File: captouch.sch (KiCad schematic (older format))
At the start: 39 parts, among them J401 MOLEX_502250-8037, J402 MOLEX_502250-8037, U401 FT5816LPC, X401 12MHz 18pF

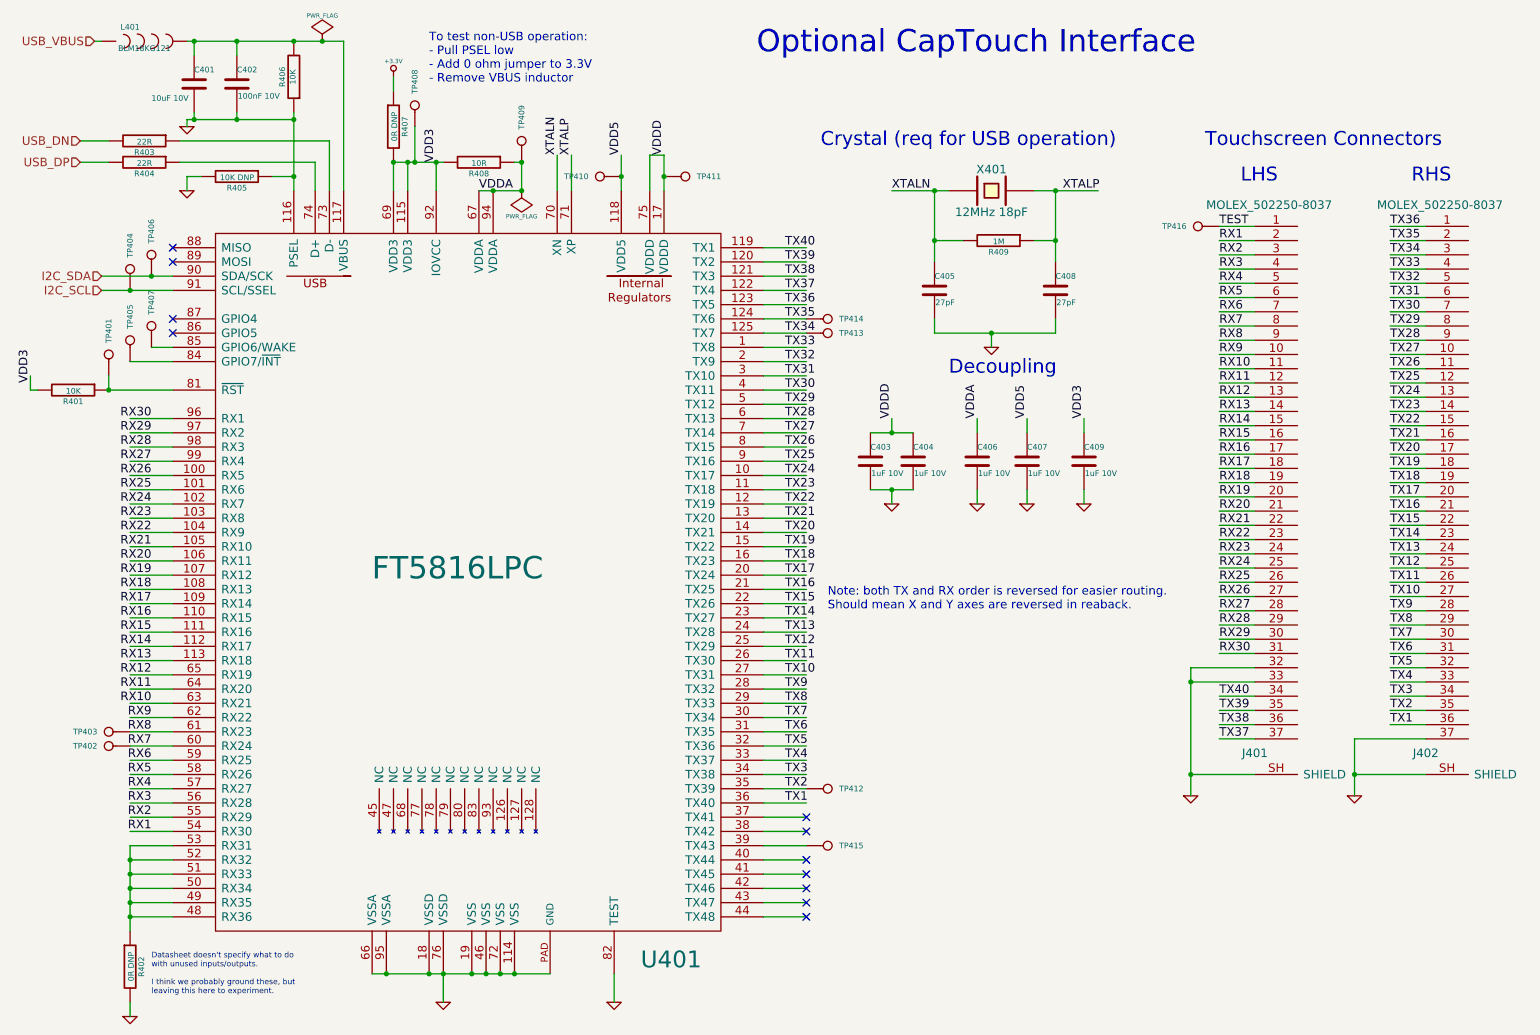
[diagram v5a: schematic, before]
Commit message: Routed, passes DRC
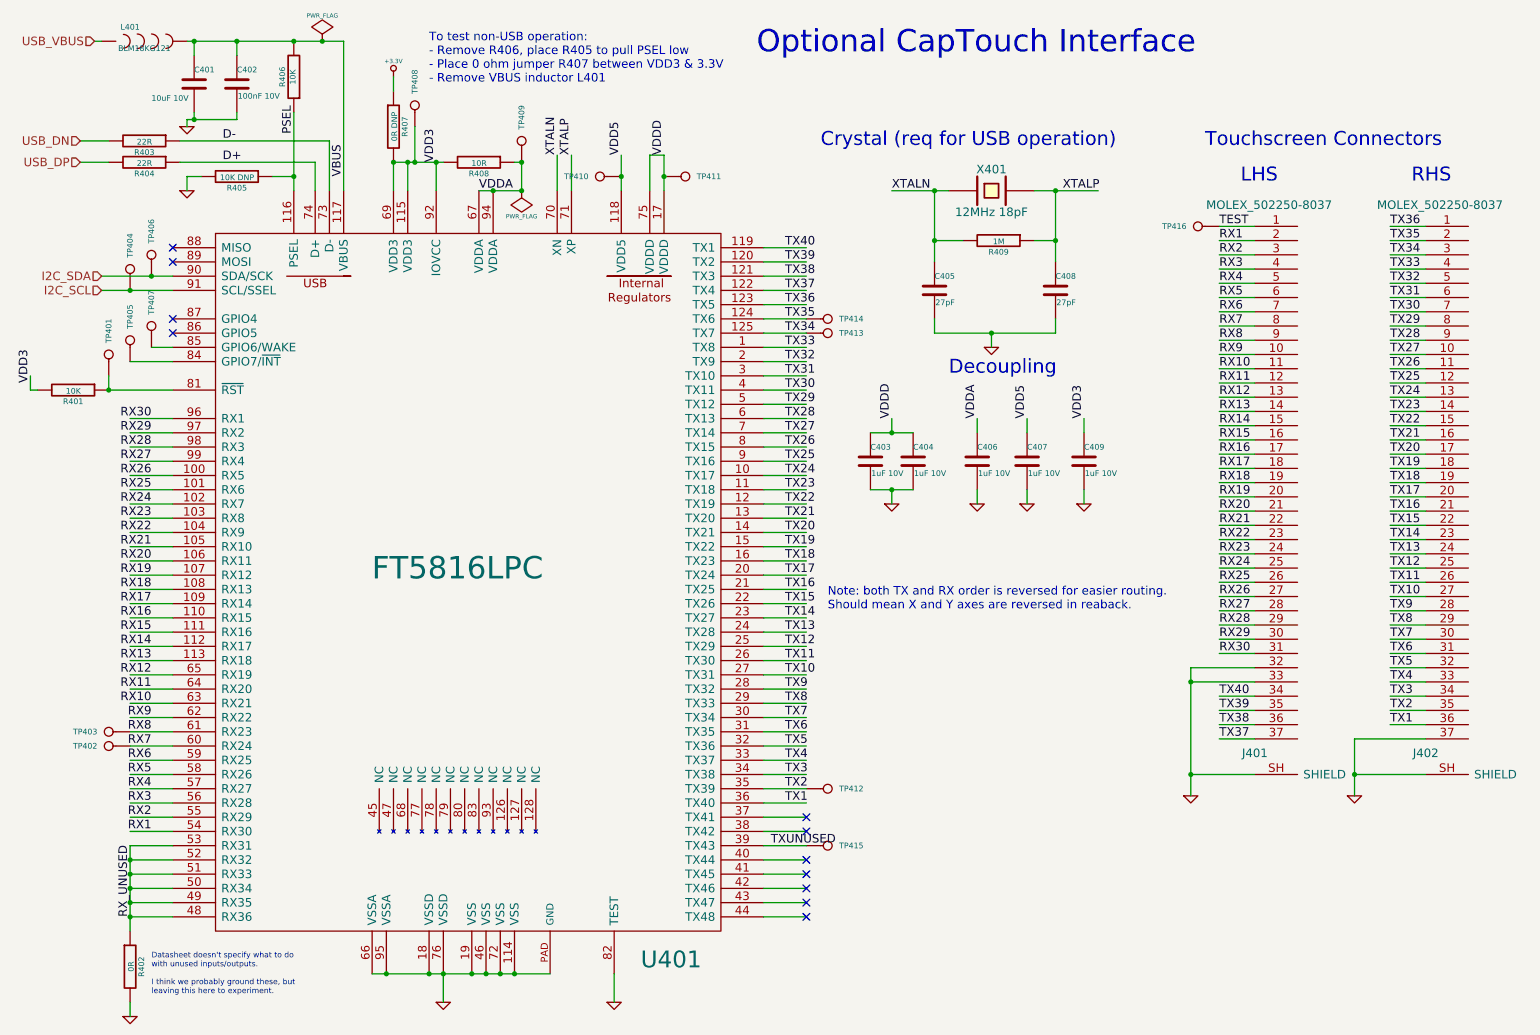
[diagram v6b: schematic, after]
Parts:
- C402: footprint SMD_Packages:SMD-0402_c -> FT:C0402
- C403, C404, C406, C407, C409: footprint FT:1206 -> FT:0603
- R402: value 0R DNP -> 0R
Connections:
- net labels added: D+, D-, PSEL, RX_UNUSED, TXUNUSED, VBUS
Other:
- note added: "To test non-USB operation:\n- Remove R406, place R405 to pull PSEL low\n- Place 0 ohm jumper R407 between VDD3 & 3.3V\n- Remove VBUS inductor L401"
- note removed: "To test non-USB operation:\n- Pull PSEL low\n- Add 0 ohm jumper to 3.3V\n- Remove VBUS inductor"
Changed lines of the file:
@@
 F 0 "C403" H 6600 3800 40  0000 L CNN
 F 1 "1uF 10V" H 6606 3615 40  0000 L CNN
-F 2 "FT:1206" H 6638 3550 30  0001 C CNN
+F 2 "FT:0603" H 6638 3550 30  0001 C CNN
 F 3 "" H 6600 3700 60  0000 C CNN
 	1    6600 3700
@@
 F 0 "C407" H 7700 3800 40  0000 L CNN
 F 1 "1uF 10V" H 7706 3615 40  0000 L CNN
-F 2 "FT:1206" H 7738 3550 30  0001 C CNN
+F 2 "FT:0603" H 7738 3550 30  0001 C CNN
 F 3 "" H 7700 3700 60  0000 C CNN
 	1    7700 3700
@@
 F 0 "C406" H 7350 3800 40  0000 L CNN
 F 1 "1uF 10V" H 7356 3615 40  0000 L CNN
-F 2 "FT:1206" H 7388 3550 30  0001 C CNN
+F 2 "FT:0603" H 7388 3550 30  0001 C CNN
 F 3 "" H 7350 3700 60  0000 C CNN
 	1    7350 3700
@@
 F 0 "C409" H 8100 3800 40  0000 L CNN
 F 1 "1uF 10V" H 8106 3615 40  0000 L CNN
-F 2 "FT:1206" H 8138 3550 30  0001 C CNN
+F 2 "FT:0603" H 8138 3550 30  0001 C CNN
 F 3 "" H 8100 3700 60  0000 C CNN
 	1    8100 3700
@@
 F 0 "C404" H 6900 3800 40  0000 L CNN
 F 1 "1uF 10V" H 6906 3615 40  0000 L CNN
-F 2 "FT:1206" H 6938 3550 30  0001 C CNN
+F 2 "FT:0603" H 6938 3550 30  0001 C CNN
 F 3 "" H 6900 3700 60  0000 C CNN
 	1    6900 3700
@@
 F 0 "C402" H 2150 1150 40  0000 L CNN
 F 1 "100nF 10V" H 2156 965 40  0000 L CNN
-F 2 "SMD_Packages:SMD-0402_c" H 2188 900 30  0001 C CNN
+F 2 "FT:C0402" H 2188 900 30  0001 C CNN
 F 3 "" H 2150 1050 60  0000 C CNN
 	1    2150 1050
@@
 	2150 750  2150 850
 Wire Wire Line
-	1800 1300 2550 1300
-Wire Wire Line
 	2150 1300 2150 1250
 Wire Wire Line
 	1850 1300 1850 1250
-Connection ~ 2150 1300
 Wire Wire Line
 	1800 1300 1800 1350
@@
 Wire Wire Line
 	1750 1450 2800 1450
-Connection ~ 2550 1300
 Wire Wire Line
 	700  3200 750  3200
@@
 RHS
 Text Notes 3500 1050 0    60   ~ 0
-To test non-USB operation:\n- Pull PSEL low\n- Add 0 ohm jumper to 3.3V\n- Remove VBUS inductor
+To test non-USB operation:\n- Remove R406, place R405 to pull PSEL low\n- Place 0 ohm jumper R407 between VDD3 & 3.3V\n- Remove VBUS inductor L401
 $Comp
 L FT5816LPC U401
@@
 P 1400 7250
 F 0 "R402" V 1480 7250 40  0000 C CNN
-F 1 "0R DNP" V 1407 7251 40  0000 C CNN
+F 1 "0R" V 1407 7251 40  0000 C CNN
 F 2 "FT:0603" V 1330 7250 30  0001 C CNN
 F 3 "" H 1400 7250 30  0000 C CNN
@@
 Text Notes 6300 4750 0    60   ~ 0
 Note: both TX and RX order is reversed for easier routing.\nShould mean X and Y axes are reversed in reaback.
+Wire Wire Line
+	1800 1300 2150 1300
+Text Label 2550 1400 1    60   ~ 0
+PSEL
+Text Label 2900 1700 1    60   ~ 0
+VBUS
+Text Label 2050 1450 0    60   ~ 0
+D-
+Text Label 2050 1600 0    60   ~ 0
+D+
+Text Label 1400 6900 1    60   ~ 0
+RX_UNUSED
+Text Label 5900 6400 0    60   ~ 0
+TXUNUSED
 $EndSCHEMATC

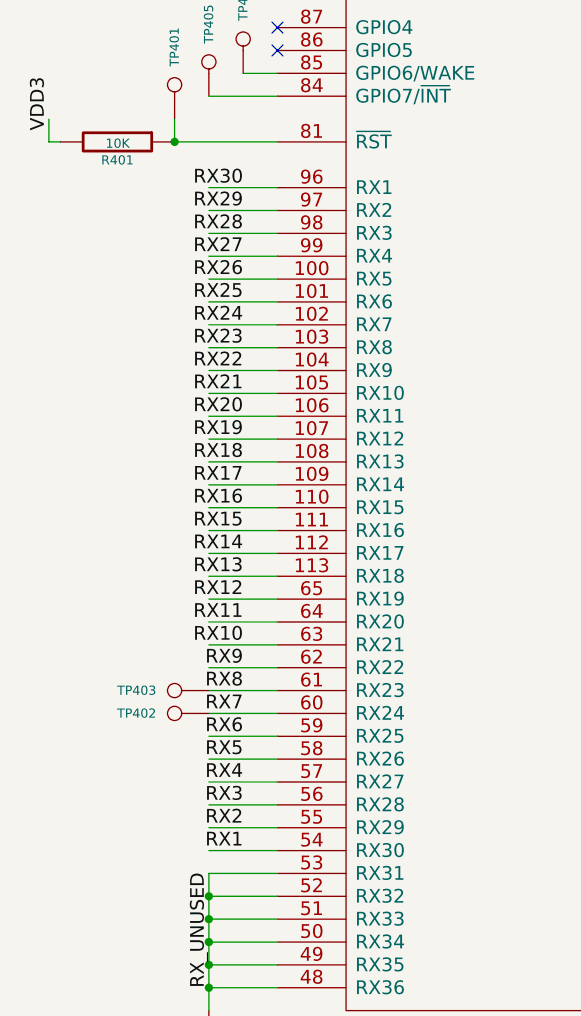
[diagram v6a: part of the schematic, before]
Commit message: More cleanup, Stencil8 mounting holes
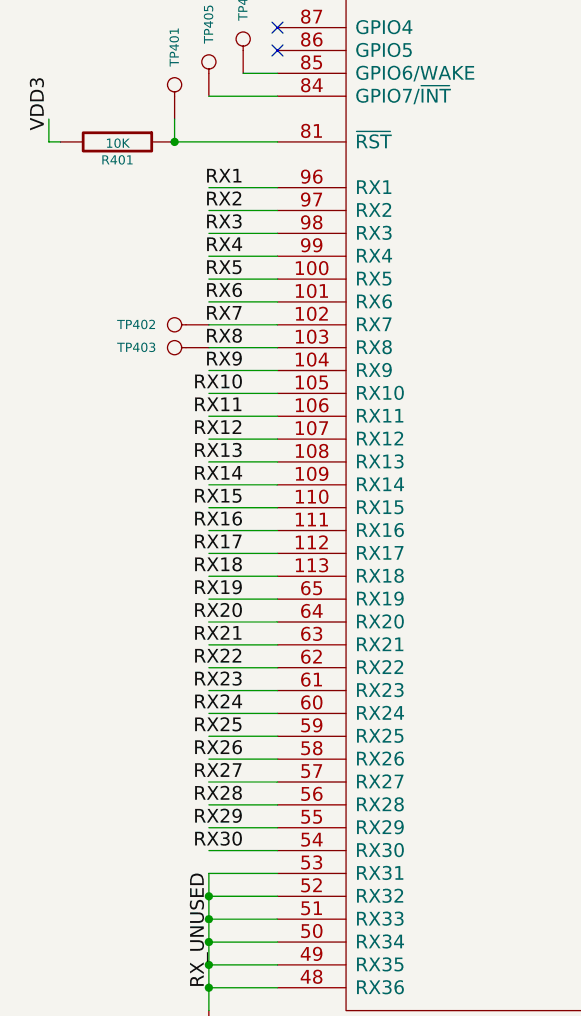
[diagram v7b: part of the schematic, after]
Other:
- moved on the sheet: TP402, TP403
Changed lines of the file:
@@
 Text Label 700  3150 1    60   ~ 0
 VDD3
+Text Label 1550 3400 2    60   ~ 0
+RX1
+Text Label 1550 3500 2    60   ~ 0
+RX2
+Text Label 1550 3600 2    60   ~ 0
+RX3
+Text Label 1550 3700 2    60   ~ 0
+RX4
+Text Label 1550 3800 2    60   ~ 0
+RX5
+Text Label 1550 3900 2    60   ~ 0
+RX6
+Text Label 1550 4000 2    60   ~ 0
+RX7
+Text Label 1550 4100 2    60   ~ 0
+RX8
+Text Label 1550 4200 2    60   ~ 0
+RX9
+Text Label 1550 4300 2    60   ~ 0
+RX10
+Text Label 1550 4400 2    60   ~ 0
+RX11
+Text Label 1550 4500 2    60   ~ 0
+RX12
+Text Label 1550 4600 2    60   ~ 0
+RX13
+Text Label 1550 4700 2    60   ~ 0
+RX14
+Text Label 1550 4800 2    60   ~ 0
+RX15
+Text Label 1550 4900 2    60   ~ 0
+RX16
+Text Label 1550 5000 2    60   ~ 0
+RX17
+Text Label 1550 5100 2    60   ~ 0
+RX18
+Text Label 1550 5200 2    60   ~ 0
+RX19
+Text Label 1550 5300 2    60   ~ 0
+RX20
+Text Label 1550 5400 2    60   ~ 0
+RX21
+Text Label 1550 5500 2    60   ~ 0
+RX22
+Text Label 1550 5600 2    60   ~ 0
+RX23
+Text Label 1550 5700 2    60   ~ 0
+RX24
+Text Label 1550 5800 2    60   ~ 0
+RX25
+Text Label 1550 5900 2    60   ~ 0
+RX26
+Text Label 1550 6000 2    60   ~ 0
+RX27
+Text Label 1550 6100 2    60   ~ 0
+RX28
+Text Label 1550 6200 2    60   ~ 0
+RX29
 Text Label 1550 6300 2    60   ~ 0
-RX1
-Text Label 1550 6200 2    60   ~ 0
-RX2
-Text Label 1550 6100 2    60   ~ 0
-RX3
-Text Label 1550 6000 2    60   ~ 0
-RX4
-Text Label 1550 5900 2    60   ~ 0
-RX5
-Text Label 1550 5800 2    60   ~ 0
-RX6
-Text Label 1550 5700 2    60   ~ 0
-RX7
-Text Label 1550 5600 2    60   ~ 0
-RX8
-Text Label 1550 5500 2    60   ~ 0
-RX9
-Text Label 1550 5400 2    60   ~ 0
-RX10
-Text Label 1550 5300 2    60   ~ 0
-RX11
-Text Label 1550 5200 2    60   ~ 0
-RX12
-Text Label 1550 5100 2    60   ~ 0
-RX13
-Text Label 1550 5000 2    60   ~ 0
-RX14
-Text Label 1550 4900 2    60   ~ 0
-RX15
-Text Label 1550 4800 2    60   ~ 0
-RX16
-Text Label 1550 4700 2    60   ~ 0
-RX17
-Text Label 1550 4600 2    60   ~ 0
-RX18
-Text Label 1550 4500 2    60   ~ 0
-RX19
-Text Label 1550 4400 2    60   ~ 0
-RX20
-Text Label 1550 4300 2    60   ~ 0
-RX21
-Text Label 1550 4200 2    60   ~ 0
-RX22
-Text Label 1550 4100 2    60   ~ 0
-RX23
-Text Label 1550 4000 2    60   ~ 0
-RX24
-Text Label 1550 3900 2    60   ~ 0
-RX25
-Text Label 1550 3800 2    60   ~ 0
-RX26
-Text Label 1550 3700 2    60   ~ 0
-RX27
-Text Label 1550 3600 2    60   ~ 0
-RX28
-Text Label 1550 3500 2    60   ~ 0
-RX29
-Text Label 1550 3400 2    60   ~ 0
 RX30
 $Comp
@@
 	700  3200 700  3100
 Wire Wire Line
+	1700 3400 1400 3400
+Wire Wire Line
+	1700 3500 1400 3500
+Wire Wire Line
+	1700 3600 1400 3600
+Wire Wire Line
+	1700 3700 1400 3700
+Wire Wire Line
+	1700 3800 1400 3800
+Wire Wire Line
+	1700 3900 1400 3900
+Wire Wire Line
+	1700 4000 1400 4000
+Wire Wire Line
+	1700 4100 1400 4100
+Wire Wire Line
+	1700 4200 1400 4200
+Wire Wire Line
+	1700 4300 1400 4300
+Wire Wire Line
+	1700 4400 1400 4400
+Wire Wire Line
+	1700 4500 1400 4500
+Wire Wire Line
+	1700 4600 1400 4600
+Wire Wire Line
+	1700 4700 1400 4700
+Wire Wire Line
+	1700 4800 1400 4800
+Wire Wire Line
+	1700 4900 1400 4900
+Wire Wire Line
+	1700 5000 1400 5000
+Wire Wire Line
+	1700 5100 1400 5100
+Wire Wire Line
+	1700 5200 1400 5200
+Wire Wire Line
+	1700 5300 1400 5300
+Wire Wire Line
+	1700 5400 1400 5400
+Wire Wire Line
+	1700 5500 1400 5500
+Wire Wire Line
+	1700 5600 1400 5600
+Wire Wire Line
+	1700 5700 1400 5700
+Wire Wire Line
+	1700 5800 1400 5800
+Wire Wire Line
+	1700 5900 1400 5900
+Wire Wire Line
+	1700 6000 1400 6000
+Wire Wire Line
+	1700 6100 1400 6100
+Wire Wire Line
+	1700 6200 1400 6200
+Wire Wire Line
 	1700 6300 1400 6300
-Wire Wire Line
-	1700 6200 1400 6200
-Wire Wire Line
-	1700 6100 1400 6100
-Wire Wire Line
-	1700 6000 1400 6000
-Wire Wire Line
-	1700 5900 1400 5900
-Wire Wire Line
-	1700 5800 1400 5800
-Wire Wire Line
-	1700 5700 1400 5700
-Wire Wire Line
-	1700 5600 1400 5600
-Wire Wire Line
-	1700 5500 1400 5500
-Wire Wire Line
-	1700 5400 1400 5400
-Wire Wire Line
-	1700 5300 1400 5300
-Wire Wire Line
-	1700 5200 1400 5200
-Wire Wire Line
-	1700 5100 1400 5100
-Wire Wire Line
-	1700 5000 1400 5000
-Wire Wire Line
-	1700 4900 1400 4900
-Wire Wire Line
-	1700 4800 1400 4800
-Wire Wire Line
-	1700 4700 1400 4700
-Wire Wire Line
-	1700 4600 1400 4600
-Wire Wire Line
-	1700 4500 1400 4500
-Wire Wire Line
-	1700 4400 1400 4400
-Wire Wire Line
-	1700 4300 1400 4300
-Wire Wire Line
-	1700 4200 1400 4200
-Wire Wire Line
-	1700 4100 1400 4100
-Wire Wire Line
-	1700 4000 1400 4000
-Wire Wire Line
-	1700 3900 1400 3900
-Wire Wire Line
-	1700 3800 1400 3800
-Wire Wire Line
-	1700 3700 1400 3700
-Wire Wire Line
-	1700 3600 1400 3600
-Wire Wire Line
-	1700 3500 1400 3500
-Wire Wire Line
-	1700 3400 1400 3400
 Wire Wire Line
 	1700 6400 1400 6400
@@
 L CONN_1 TP402
 U 1 1 5447C3A6
-P 1250 5700
-F 0 "TP402" H 1330 5700 40  0000 L CNN
-F 1 "CONN_1" H 1250 5755 30  0001 C CNN
-F 2 "novepad:SMD_TEST_POINT" H 1250 5700 60  0001 C CNN
-F 3 "" H 1250 5700 60  0000 C CNN
-	1    1250 5700
-	-1   0    0    -1
+P 1250 4000
+F 0 "TP402" H 1330 4000 40  0000 L CNN
+F 1 "CONN_1" H 1250 4055 30  0001 C CNN
+F 2 "novepad:SMD_TEST_POINT" H 1250 4000 60  0001 C CNN
+F 3 "" H 1250 4000 60  0000 C CNN
+	1    1250 4000
+	-1   0    0    1
 $EndComp
 $Comp
 L CONN_1 TP403
 U 1 1 5447C963
-P 1250 5600
-F 0 "TP403" H 1330 5600 40  0000 L CNN
-F 1 "CONN_1" H 1250 5655 30  0001 C CNN
-F 2 "novepad:SMD_TEST_POINT" H 1250 5600 60  0001 C CNN
-F 3 "" H 1250 5600 60  0000 C CNN
-	1    1250 5600
-	-1   0    0    -1
-$EndComp
-$Comp
+P 1250 4100
+F 0 "TP403" H 1330 4100 40  0000 L CNN
+F 1 "CONN_1" H 1250 4155 30  0001 C CNN
+F 2 "novepad:SMD_TEST_POINT" H 1250 4100 60  0001 C CNN
+F 3 "" H 1250 4100 60  0000 C CNN
+	1    1250 4100
+	-1   0    0    1
+$EndComp
+$Comp
